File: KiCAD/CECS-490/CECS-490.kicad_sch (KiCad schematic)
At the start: 37 parts, among them M1 Motor_DC, Q1 IRLZ44N, U1 74HC595, U2 TM4C1230H6PM, U3 74HC595

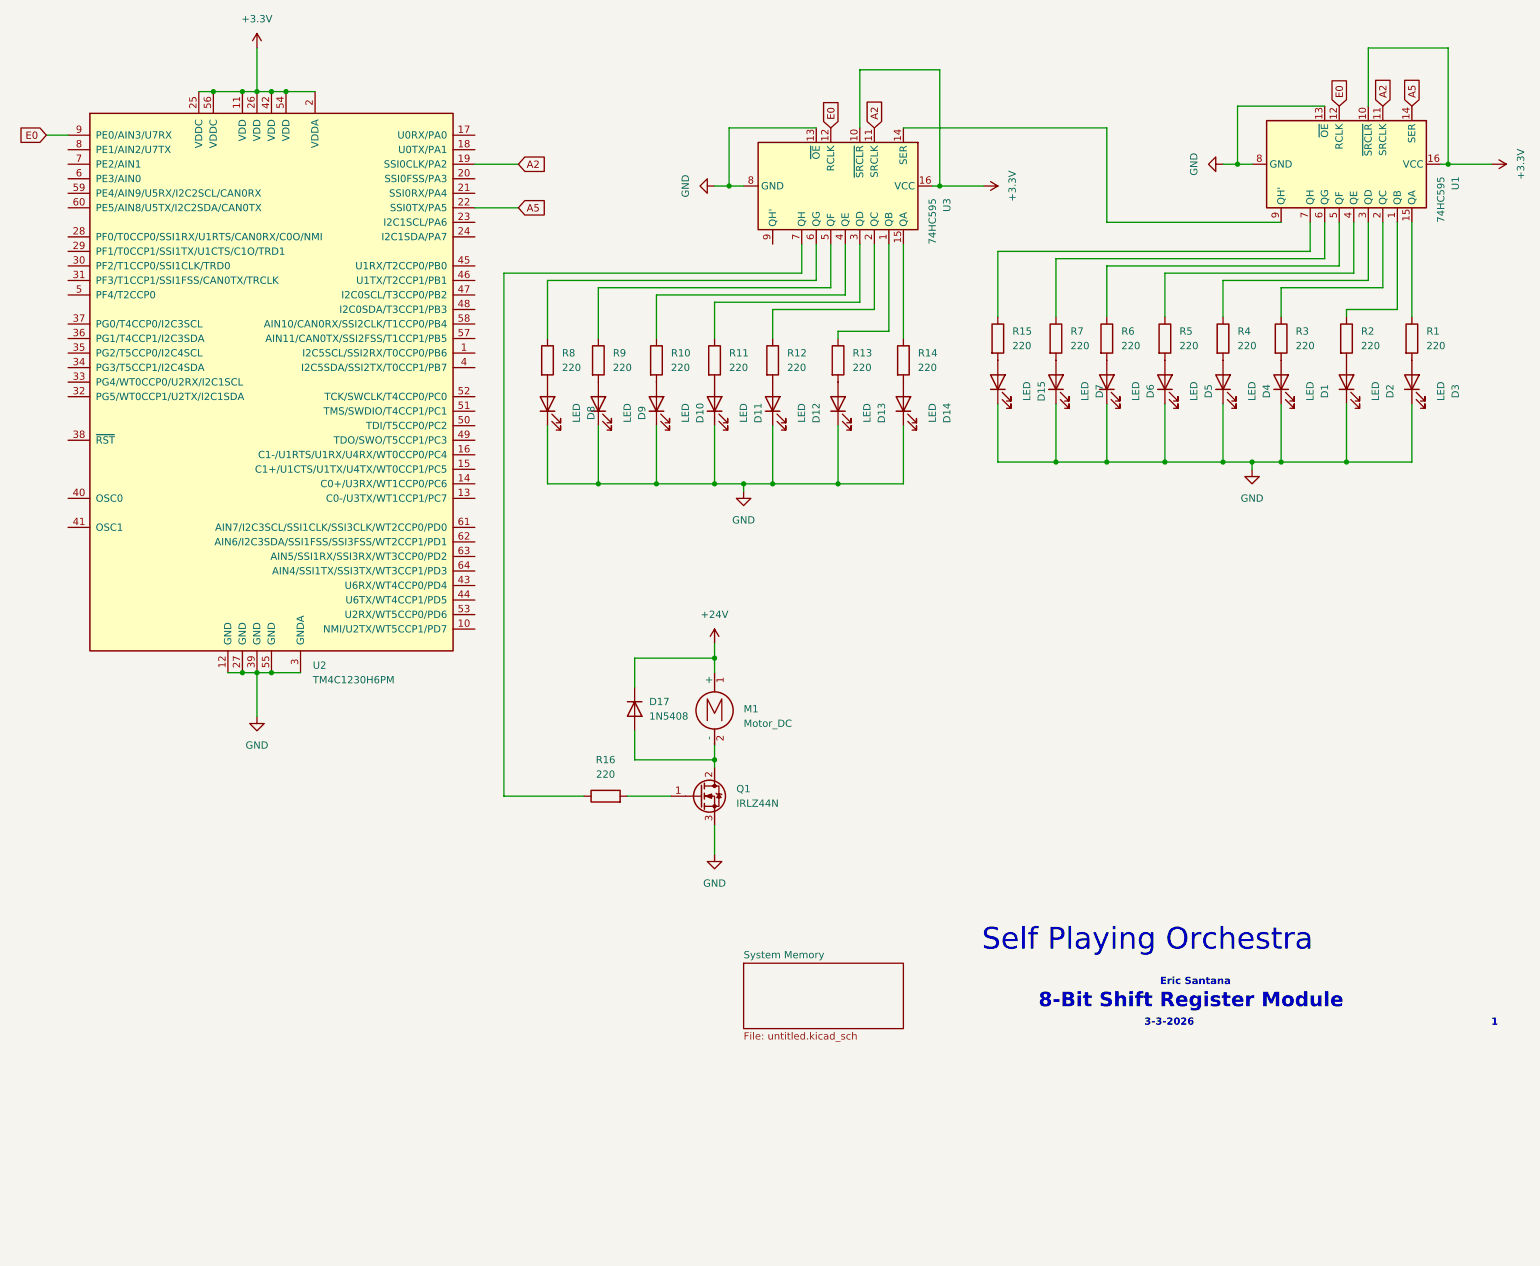
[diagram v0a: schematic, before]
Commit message: Added support circuit for MCU
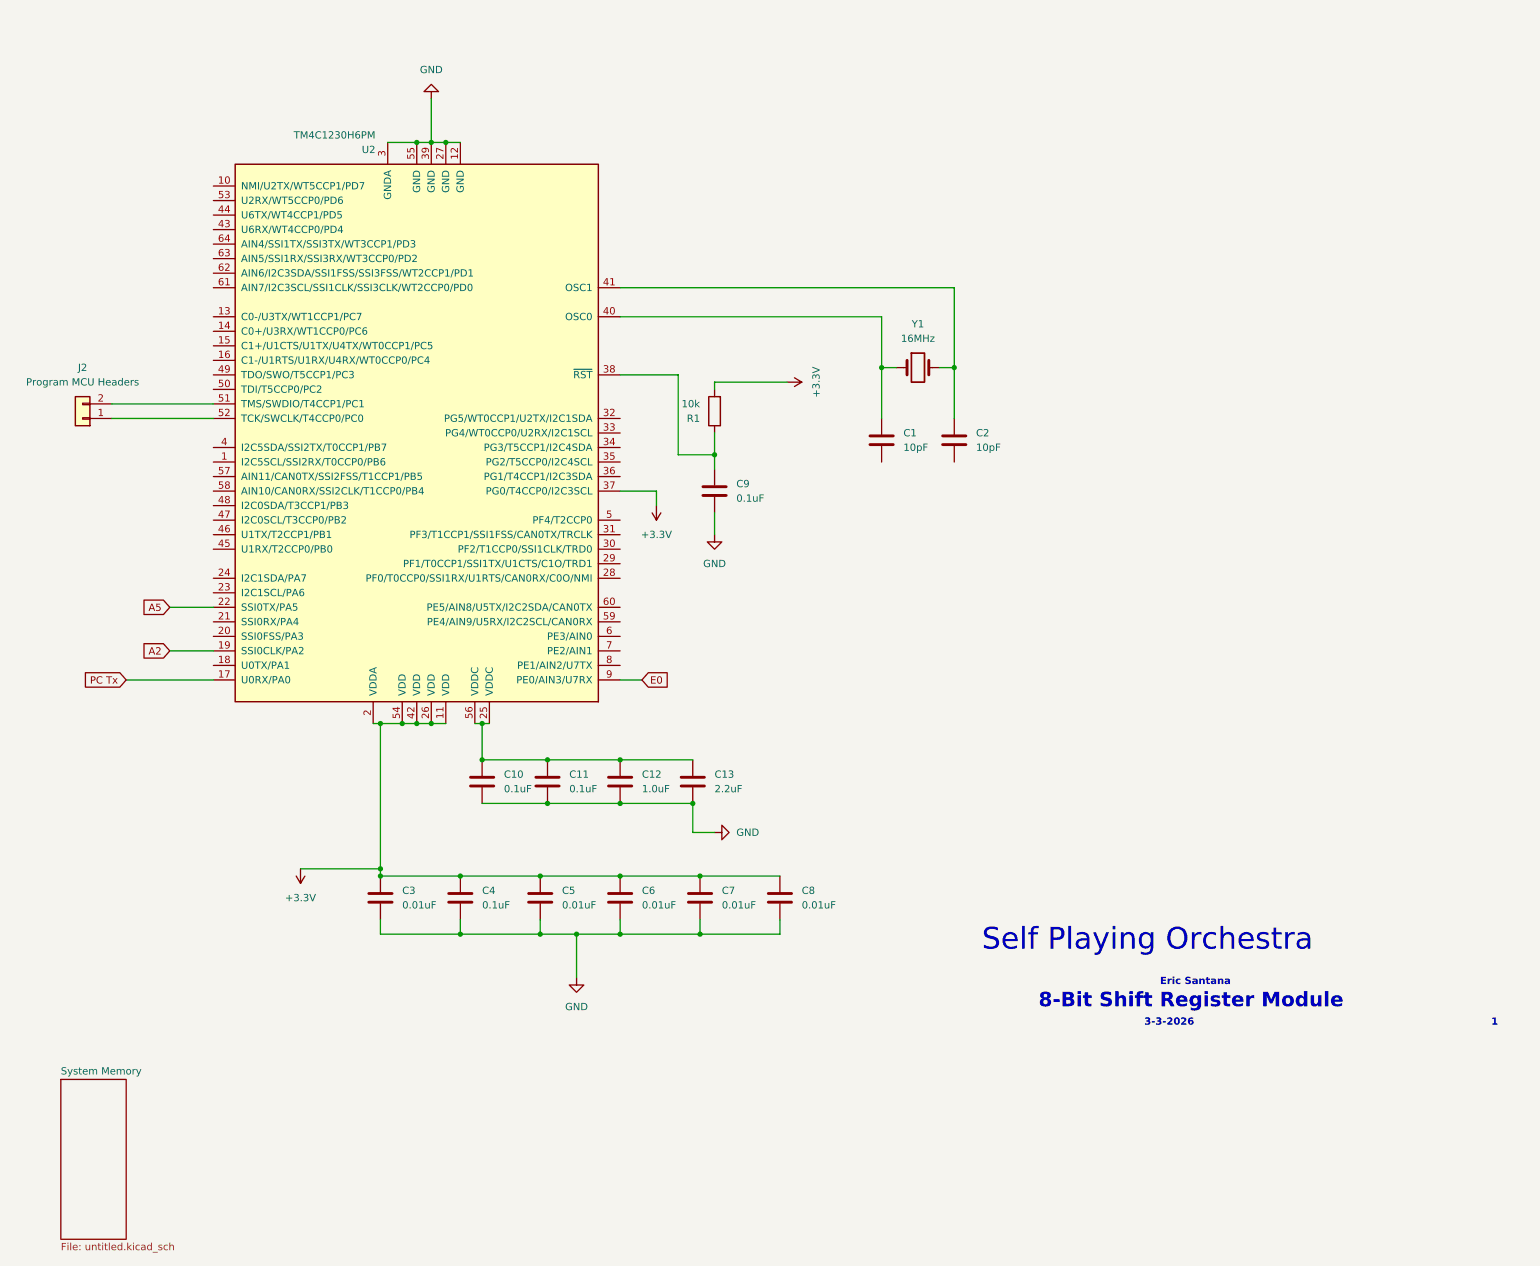
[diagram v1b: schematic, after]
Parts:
- removed D1, D10, D11, D12, D13, D14, D15, D2, D3, D4, D5, D6, D7, D8, D9: LED, symbol Device:LED
- removed D17: 1N5408, Diode_THT:D_DO-201AD_P15.24mm_Horizontal, symbol Diode:1N5408
- removed M1: Motor_DC, symbol Motor:Motor_DC
- removed Q1: IRLZ44N, Package_TO_SOT_THT:TO-220-3_Vertical, symbol Transistor_FET:IRLZ44N
- removed R10, R11, R12, R13, R14, R15, R16, R2, R3, R4, R5, R6, R7, R8, R9: 220, symbol Device:R
- removed U1, U3: 74HC595, symbol 74xx:74HC595
- added C1, C2: 10pF, symbol Device:C
- added C10, C11, C4, C9: 0.1uF, symbol Device:C
- added C12: 1.0uF, symbol Device:C
- added C13: 2.2uF, symbol Device:C
- added C3, C5, C6, C7, C8: 0.01uF, symbol Device:C
- added J2: Program MCU Headers, symbol Connector_Generic:Conn_01x02
- added Y1: 16MHz, symbol Device:Crystal
- R1: value 220 -> 10k
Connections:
- net +3.3V: now also R1.2, U2.37 (PG0/T4CCP0/I2C3SCL), C3.1, C4.1, C5.1, C6.1, C7.1, C8.1; no longer U2.25 (VDDC), U2.56 (VDDC)
- net GND: now also C10.2, C11.2, C12.2, C13.2, C3.2, C4.2, C5.2, C6.2, C7.2, C8.2, C9.2
- net at R1.1: now also U2.38 (~{RST}), C9.1
- net PC Tx: now reaches U2.17 (U0RX/PA0)
- net at U2.40 (OSC0): now also C1.1, Y1.1
- net at U2.41 (OSC1): now also C2.1, Y1.2
- net at U2.51 (TMS/SWDIO/T4CCP1/PC1): now also J2.2 (Pin_2)
- net at U2.52 (TCK/SWCLK/T4CCP0/PC0): now also J2.1 (Pin_1)
- new net: C10.1, C11.1, C12.1, C13.1, U2.25 (VDDC), U2.56 (VDDC)
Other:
- moved on the sheet: U2
